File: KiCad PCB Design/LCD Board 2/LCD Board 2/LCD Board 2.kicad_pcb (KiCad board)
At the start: 2 copper layers, 27.9 x 27.9 mm, 8 parts, among them J1 Conn_01x03_Male, J2 Conn_01x03_Male, J3 Conn_01x02_Male, U1 ATtiny412-SS

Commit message: v1.9 - KiCad LCD Board Updates
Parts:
- added J4: Conn_PinHeader_1x07_P2.54mm_Horizontal_SMD, fab:PinHeader_1x07_P2.54mm_Horizontal_SMD, F.Cu at (169.2, 118.1)
- J1: value Conn_01x03_Male -> Conn_PinHeader_1x04_P2.54mm_Horizontal_SMD; footprint fab:PinHeader_1x03_P2.54mm_Horizontal_SMD -> fab:PinHeader_1x04_P2.54mm_Horizontal_SMD
- J2: value Conn_01x03_Male -> Conn_PinHeader_1x10_P2.54mm_Horizontal_SMD; footprint fab:PinHeader_1x03_P2.54mm_Horizontal_SMD -> fab:PinHeader_1x10_P2.54mm_Horizontal_SMD
- J3: value Conn_01x02_Male -> Conn_PinHeader_1x02_P2.54mm_Horizontal_SMD; footprint fab:PinHeader_1x02_P2.54mm_Horizontal_SMD -> fab:PinHeader_UPDI_01x02_P2.54mm_Horizontal_SMD
- U1: value ATtiny412-SS -> Microcontroller_ATtiny1614-SSFR; footprint Package_SO:SOIC-8_3.9x4.9mm_P1.27mm -> fab:SOIC-14_3.9x8.7mm_P1.27mm
- moved R1 30.2 mm to (163.8, 125.7), turned to 180 degrees
- moved J1 25.8 mm to (165.1, 129.1), turned to -90 degrees
- moved D1 21.1 mm to (163.8, 120.7)
- moved R3 21.1 mm to (163.8, 118.1), turned to 0 degrees
- moved J3 20.1 mm to (153.7, 129.1)
- moved R2 19.9 mm to (163.8, 123.2), turned to 180 degrees
- moved U1 19.8 mm to (154.9, 121.9)
- moved J2 17.1 mm to (151.1, 114.1)
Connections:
- J1 pad 1: Net-(J1-Pad1) -> Net-(R1-Pad2)
- J1 pad 2: Net-(J1-Pad2) -> Net-(R1-Pad2)
- J1 pad 3: Net-(J1-Pad2) -> Net-(J1-Pad3)
- J2 pad 1: Net-(J2-Pad1) -> Net-(R3-Pad1)
- J2 pad 2: Net-(J2-Pad1) -> Net-(R3-Pad1)
- J2 pad 3: Net-(J2-Pad1) -> Net-(R3-Pad1)
- R1 pad 1: Net-(J3-Pad2) -> Net-(R1-Pad1)
- R1 pad 2: Net-(J1-Pad2) -> Net-(R1-Pad2)
- R2 pad 1: Net-(J3-Pad1) -> Net-(R1-Pad1)
- R2 pad 2: Net-(J1-Pad2) -> Net-(J1-Pad3)
- R3 pad 1: Net-(D1-Pad1) -> Net-(R3-Pad1)
- R3 pad 2: Net-(J2-Pad1) -> Net-(D1-Pad1)
- U1 pad 1: Net-(J1-Pad2) -> Net-(J3-Pad2)
- U1 pad 4: Net-(J3-Pad2) -> unconnected-(U1-Pad4)
- U1 pad 5: Net-(J3-Pad1) -> unconnected-(U1-Pad5)
- U1 pad 6: Net-(J1-Pad1) -> unconnected-(U1-Pad6)
- U1 pad 7: Net-(D1-Pad2) -> unconnected-(U1-Pad7)
- U1 pad 8: Net-(J2-Pad1) -> Net-(R1-Pad2)
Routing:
- net Net-(J1-Pad2): track 32.5 -> 0.00 mm
- net Net-(R3-Pad1): track 0.00 -> 31.6 mm
- net Net-(R1-Pad1): track 0.00 -> 21.9 mm
- net Net-(J1-Pad3): track 0.00 -> 14.7 mm
- net Net-(J2-Pad1): track 12.2 -> 0.00 mm
- net Net-(R1-Pad2): track 0.00 -> 10.7 mm
- net Net-(J3-Pad2): track 7.07 -> 13.4 mm
- net Net-(J1-Pad1): track 5.96 -> 0.00 mm
- net Net-(J3-Pad1): track 6.99 -> 8.22 mm
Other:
- board size 27.9 x 27.9 mm -> 30.5 x 31.8 mm

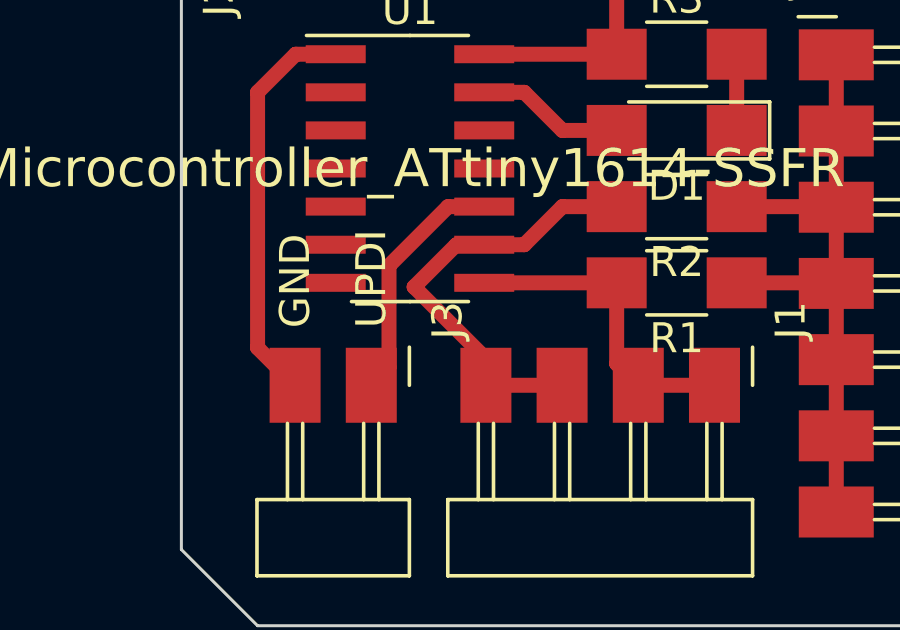
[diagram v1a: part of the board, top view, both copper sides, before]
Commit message: v2.0 - i2C Testing Boards Designed
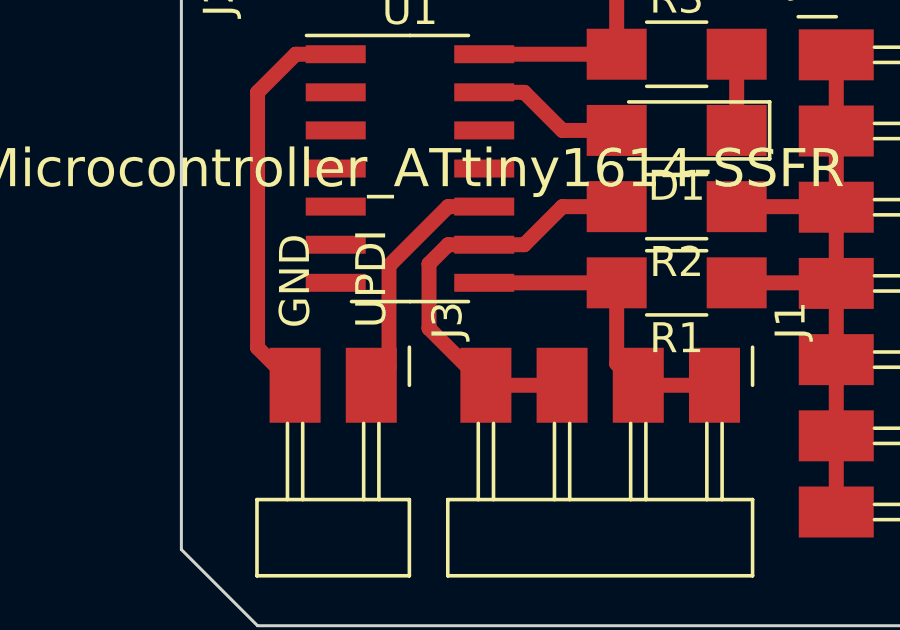
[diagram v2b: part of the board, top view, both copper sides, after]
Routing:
- net Net-(J1-Pad3): track 14.7 -> 15.3 mm
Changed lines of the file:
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@@
       (effects (font (size 1 1) (thickness 0.15)))
     )
-    (fp_text value "R" (at 0 1.9) (layer "F.Fab")
+    (fp_text value "R" (at 10.16 1.27) (layer "F.Fab")
       (effects (font (size 1 1) (thickness 0.15)))
     )
@@
       (effects (font (size 1 1) (thickness 0.15)))
     )
-    (fp_text value "R" (at 0 1.9) (layer "F.Fab")
+    (fp_text value "R" (at -10.16 3.81) (layer "F.Fab")
       (effects (font (size 1 1) (thickness 0.15)))
     )
@@
       (effects (font (size 1 1) (thickness 0.15)))
     )
-    (fp_text value "LED" (at 0 1.9) (layer "F.Fab")
+    (fp_text value "LED" (at -10.16 1.27) (layer "F.Fab")
       (effects (font (size 1 1) (thickness 0.15)))
     )
@@
       (effects (font (size 1 1) (thickness 0.15)))
     )
-    (fp_text value "R" (at 0 1.9) (layer "F.Fab")
+    (fp_text value "R" (at -10.16 6.35) (layer "F.Fab")
       (effects (font (size 1 1) (thickness 0.15)))
     )
@@
   (gr_line (start 149.86 105.41) (end 149.86 105.41) (layer "Edge.Cuts") (width 0.1))
   (segment (start 157.47 128.26) (end 157.47 129.145) (width 0.5) (layer "F.Cu") (net 1))
-  (segment (start 157.415 124.46) (end 156.485978 124.46) (width 0.5) (layer "F.Cu") (net 1))
   (segment (start 158.75 124.46) (end 160.02 123.19) (width 0.5) (layer "F.Cu") (net 1))
   (segment (start 157.47 129.145) (end 160.01 129.145) (width 0.5) (layer "F.Cu") (net 1))
-  (segment (start 155.077989 125.867989) (end 157.47 128.26) (width 0.5) (layer "F.Cu") (net 1))
-  (segment (start 156.485978 124.46) (end 155.077989 125.867989) (width 0.5) (layer "F.Cu") (net 1))
+  (segment (start 156.21 124.46) (end 155.575 125.095) (width 0.5) (layer "F.Cu") (net 1))
+  (segment (start 155.575 125.095) (end 155.575 127.25) (width 0.5) (layer "F.Cu") (net 1))
+  (segment (start 157.415 124.46) (end 156.21 124.46) (width 0.5) (layer "F.Cu") (net 1))
+  (segment (start 155.575 127.25) (end 157.47 129.145) (width 0.5) (layer "F.Cu") (net 1))
   (segment (start 157.415 124.46) (end 158.75 124.46) (width 0.5) (layer "F.Cu") (net 1))
   (segment (start 160.02 123.19) (end 161.83 123.19) (width 0.5) (layer "F.Cu") (net 1))
